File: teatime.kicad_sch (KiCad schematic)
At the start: 29 parts, among them J1 I2C, J2 UPDI, SW3 C&K PTS526, SW4 C&K PTS526, U1 GoodDisplay_GDC04212, U2 ATtiny417-M, Y1 32.768kHz 12.5pF

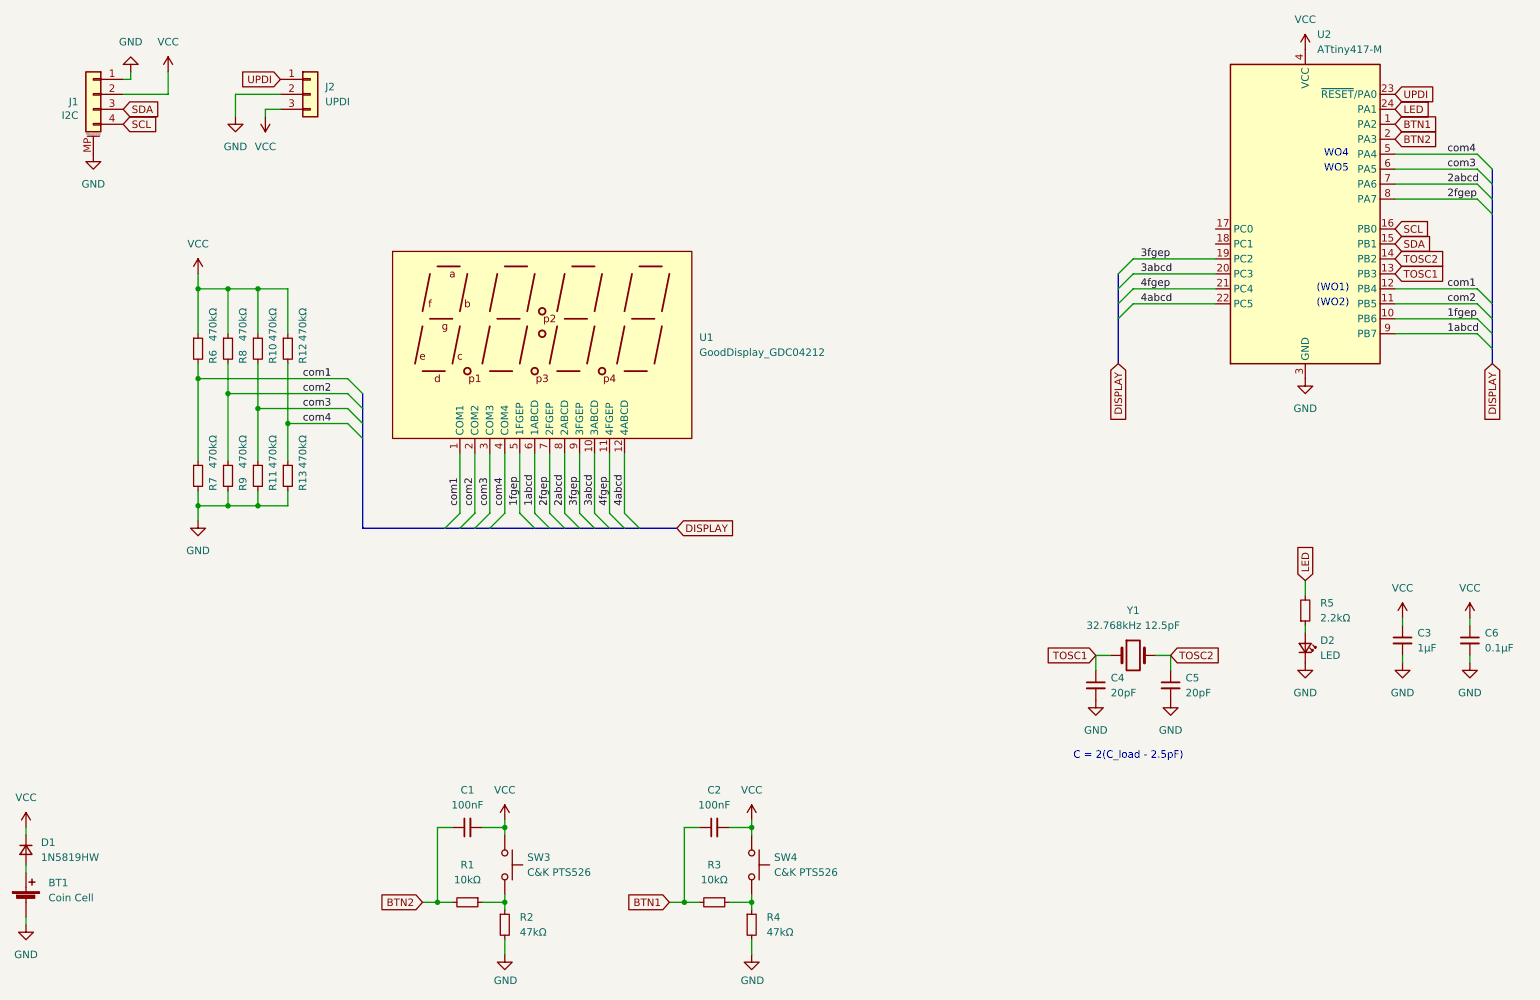
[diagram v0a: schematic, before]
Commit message: updated design using dedicated rohm BU9796AMUV driver
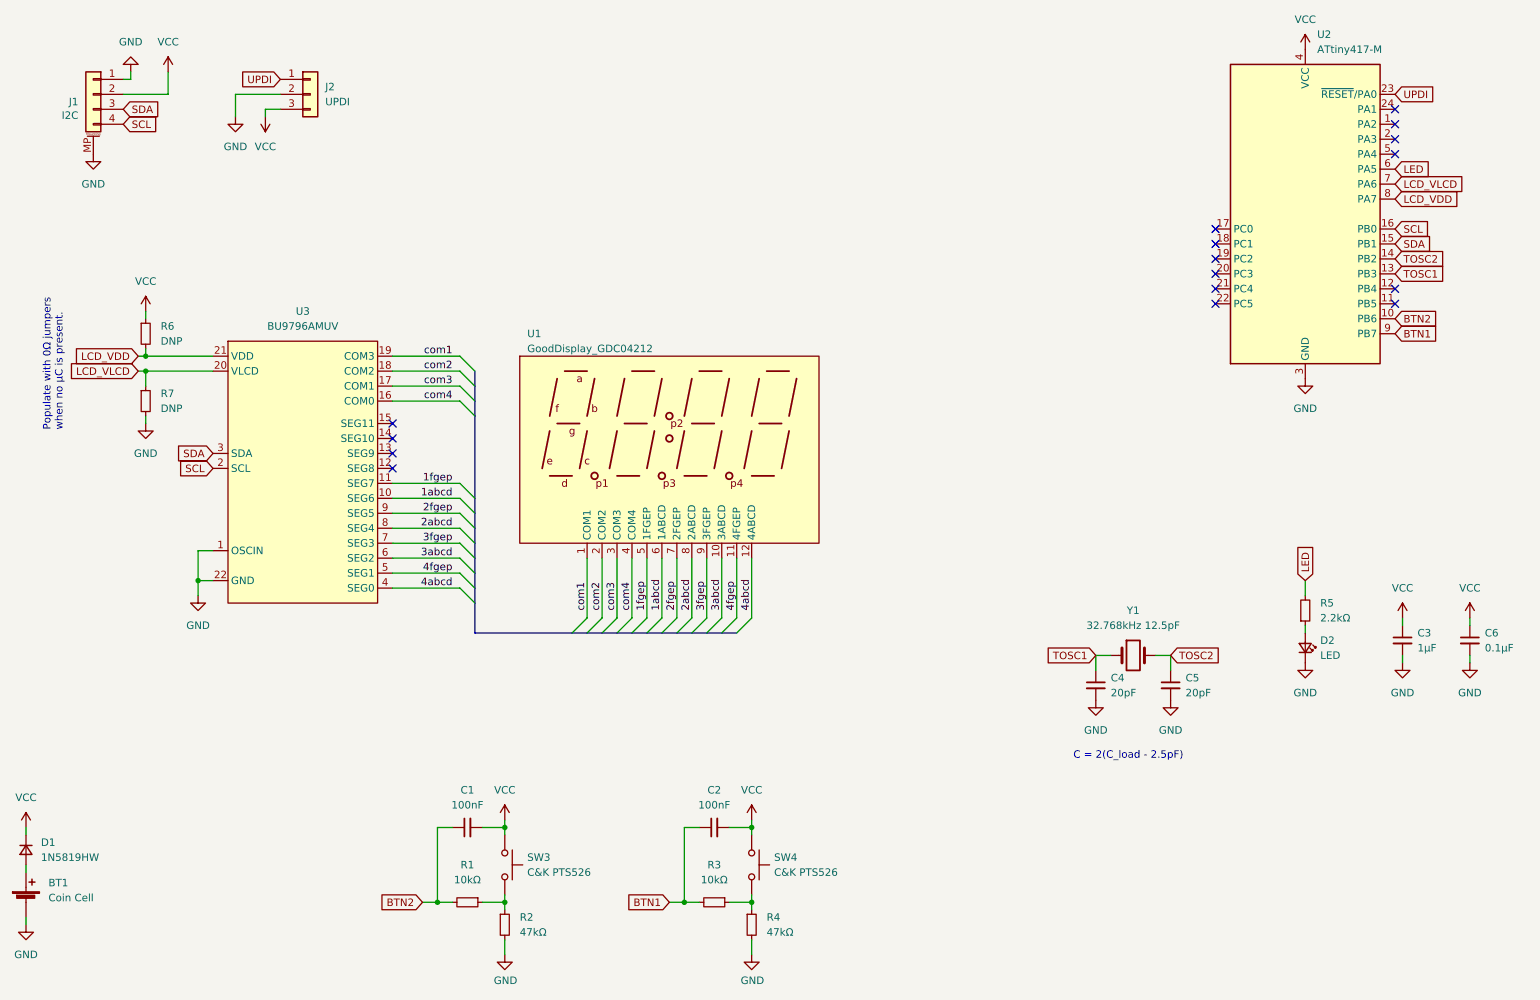
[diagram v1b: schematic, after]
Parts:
- removed R10, R11, R12, R13, R8, R9: 470kΩ, Resistor_SMD:R_0805_2012Metric, symbol Device:R_Small
- added U3: BU9796AMUV, Package_DFN_QFN:VQFN-24-1EP_4x4mm_P0.5mm_EP2.45x2.45mm, symbol local:BU9796AMUV
- R6, R7: value 470kΩ -> DNP
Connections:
- net 1abcd: now also U3.10 (SEG6); no longer U2.9 (PB7)
- net 1fgep: now also U3.11 (SEG7); no longer U2.10 (PB6)
- net 2abcd: now also U3.8 (SEG4); no longer U2.7 (PA6)
- net 2fgep: now also U3.9 (SEG5); no longer U2.8 (PA7)
- net 3abcd: now also U3.6 (SEG2); no longer U2.20 (PC3)
- net 3fgep: now also U3.7 (SEG3); no longer U2.19 (PC2)
- net 4abcd: now also U3.4 (SEG0); no longer U2.22 (PC5)
- net 4fgep: now also U3.5 (SEG1); no longer U2.21 (PC4)
- net BTN1: now also U2.9 (PB7); no longer U2.1 (PA2)
- net BTN2: now also U2.10 (PB6); no longer U2.2 (PA3)
- net GND: now also U3.1 (OSCIN), U3.22 (GND), U3.23 (TEST1), U3.24 (TEST2), U3.25 (EXT-PAD)
- net LED: now also U2.6 (PA5); no longer U2.24 (PA1)
- net SCL: now also U3.2 (SCL)
- net SDA: now also U3.3 (SDA)
- net com1: now also U3.19 (COM3); no longer R6.2, R7.1, U2.12 (PB4)
- net com2: now also U3.18 (COM2); no longer U2.11 (PB5)
- net com3: now also U3.17 (COM1); no longer U2.6 (PA5)
- net com4: now also U3.16 (COM0); no longer U2.5 (PA4)
- new net LCD_VDD: R6.2, U2.8 (PA7), U3.21 (VDD)
- new net LCD_VLCD: R7.1, U2.7 (PA6), U3.20 (VLCD)
- no-connect marks 0 -> 16
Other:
- note added: "Populate with 0Ω jumpers when no µC is present."
- note removed: "(WO1)"
- note removed: "(WO2)"
- note removed: "WO4"
- note removed: "WO5"
- moved on the sheet: U1
